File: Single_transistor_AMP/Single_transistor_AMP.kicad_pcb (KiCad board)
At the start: 2 copper layers, 0 parts

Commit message: Majasdarbs peec 8. lekcijas, kur jauzzimee plate
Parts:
- added C1: 1 uF, Capacitors_THT:CP_Axial_L10.0mm_D4.5mm_P15.00mm_Horizontal, F.Cu at (98.2, 145.4)
- added C2: 20 uF, Capacitors_THT:CP_Radial_D10.0mm_P2.50mm, F.Cu at (112.3, 127.6)
- added J1: Barosana un ieeja, Connectors:AK300-4, F.Cu at (113.7, 154.8)
- added J2: Izeja, Connectors:AK300-2, F.Cu at (95.5, 126.7)
- added J3: Stiprinajums1, Mounting_Holes:MountingHole_2.2mm_M2_Pad, F.Cu at (121.7, 146.1)
- added J4: Stiprinajums2, Mounting_Holes:MountingHole_2.2mm_M2_Pad, F.Cu at (93.5, 145.4)
- added J5: Stiprinajums3, Mounting_Holes:MountingHole_2.2mm_M2_Pad, F.Cu at (106.8, 122.8)
- added Q1: BC547, TO_SOT_Packages_THT:TO-92_Molded_Narrow, F.Cu at (106.3, 138.2)
- added R1: 4.7 k, Resistors_THT:R_Axial_DIN0204_L3.6mm_D1.6mm_P7.62mm_Horizontal, F.Cu at (86.4, 141.2)
- added R2: 1k, Resistors_THT:R_Axial_DIN0207_L6.3mm_D2.5mm_P10.16mm_Horizontal, F.Cu at (124.5, 141.6)
- added R3: 4.7 k, Resistors_THT:R_Axial_DIN0204_L3.6mm_D1.6mm_P7.62mm_Horizontal, F.Cu at (86.4, 135.9)
- added R4: 1 k, Resistors_THT:R_Axial_DIN0207_L6.3mm_D2.5mm_P10.16mm_Horizontal, F.Cu at (124.5, 136.7)
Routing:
- net Net-(C1-Pad1): track 0.00 -> 43.6 mm
- net Net-(C2-Pad2): track 0.00 -> 28.4 mm
- net +9V: track 0.00 -> 25.9 mm
- net Net-(J2-Pad1): track 0.00 -> 25.3 mm
- net Net-(C1-Pad2): track 0.00 -> 9.61 mm
- added copper zone on B.Cu, net GND
- added copper zone on F.Cu, net GND
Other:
- board outline added: 50 x 43.3 mm

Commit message: Single_transistor_AMP 2. iteraacija
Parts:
- C1: footprint Capacitors_THT:CP_Axial_L10.0mm_D4.5mm_P15.00mm_Horizontal -> Capacitors_THT:C_Rect_L10.0mm_W2.5mm_P7.50mm_MKS4
- C2: footprint Capacitors_THT:CP_Radial_D10.0mm_P2.50mm -> Capacitors_THT:C_Rect_L10.0mm_W2.5mm_P7.50mm_MKS4
- moved R4 10.5 mm to (113.9, 136.9), turned to 0 degrees
- moved R2 10.4 mm to (114.0, 141.5), turned to 0 degrees
- moved C2 10.3 mm to (122.2, 130.3), turned to 180 degrees
- moved C1 5.58 mm to (103.2, 143.1)
- moved J4 4.05 mm to (90.8, 148.5), turned to 0 degrees
- moved J3 2.50 mm to (121.0, 148.5), turned to 0 degrees
- moved J5 1.45 mm to (108.2, 122.4)
- moved Q1 0.80 mm to (106.6, 137.4)
- moved J1 0.51 mm to (113.7, 154.3)
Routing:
- net Net-(C2-Pad2): track 28.4 -> 12.0 mm
- net Net-(C1-Pad1): track 43.6 -> 27.2 mm
- net Net-(J2-Pad1): track 25.3 -> 23.0 mm
- net Net-(C1-Pad2): track 9.61 -> 11.4 mm
- net +9V: track 25.9 -> 24.4 mm

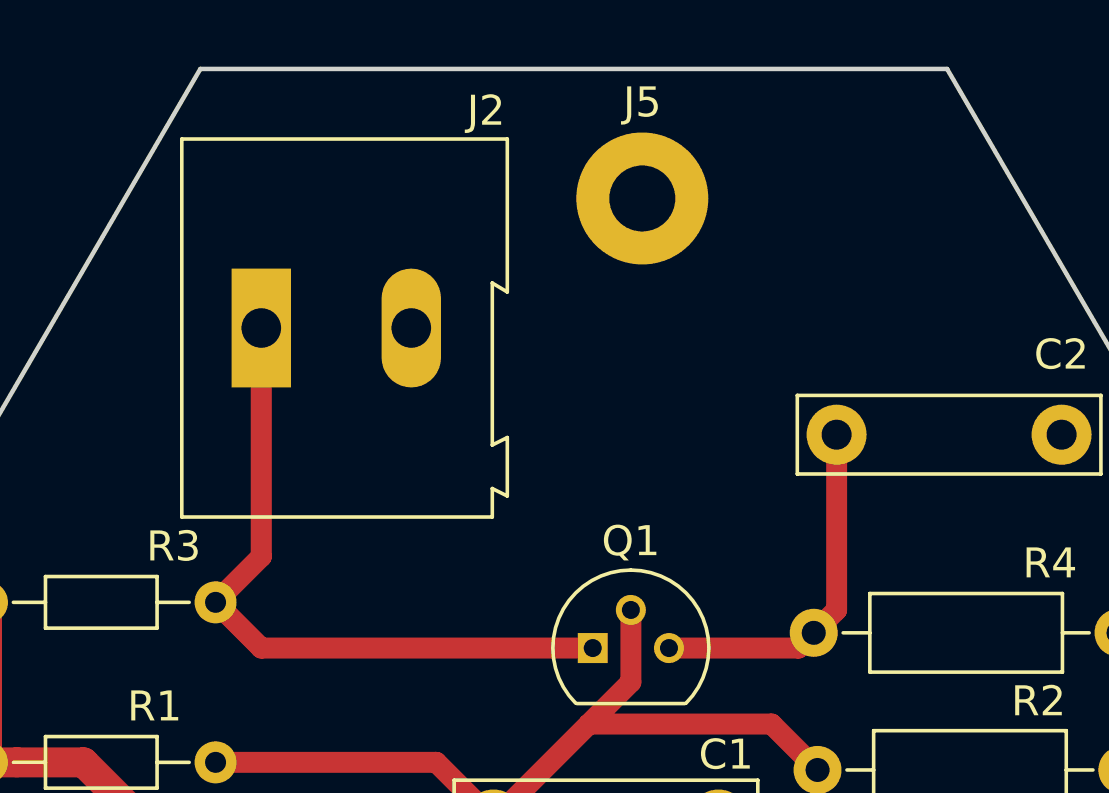
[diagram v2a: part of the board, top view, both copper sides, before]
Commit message: Single transistor AMP 2. iteraacija
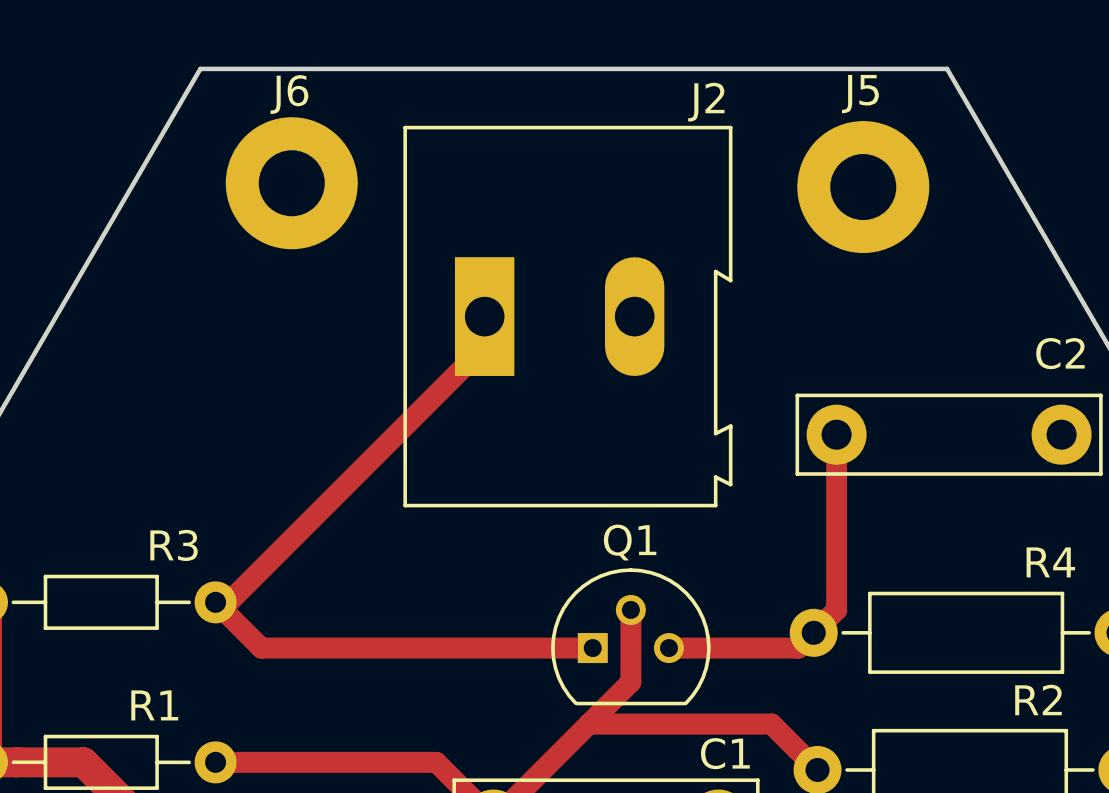
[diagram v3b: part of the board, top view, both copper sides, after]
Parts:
- added J6: Stiprinajums4, Mounting_Holes:MountingHole_2.2mm_M2_Pad, F.Cu at (96.5, 121.9)
- moved J2 7.46 mm to (103.0, 126.4)
- moved J5 7.38 mm to (115.6, 122.0)
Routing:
- net Net-(J2-Pad1): track 23.0 -> 26.7 mm
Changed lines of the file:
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@@
 (kicad_pcb (version 4) (host pcbnew 4.0.7)
   (general
-    (links 18)
+    (links 19)
     (no_connects 0)
     (area 80.823999 118.034999 131.012001 161.492001)
     (thickness 1.6)
     (drawings 6)
-    (tracks 22)
+    (tracks 23)
     (zones 0)
-    (modules 12)
+    (modules 13)
     (nets 7)
   )
@@
   )
   (module Connectors:AK300-2 (layer F.Cu)
-    (at 95.504 126.746)
+    (at 102.95 126.365)
     (descr CONNECTOR)
     (tags CONNECTOR)
@@
   )
   (module Mounting_Holes:MountingHole_2.2mm_M2_Pad (layer F.Cu)
-    (at 108.204 122.428)
+    (at 115.57 122.047)
     (descr "Mounting Hole 2.2mm, M2")
     (tags "mounting hole 2.2mm m2")
@@
       (rotate (xyz 0 0 0))
     )
+  )
+  (module Mounting_Holes:MountingHole_2.2mm_M2_Pad (layer F.Cu)
+    (at 96.52 121.92)
+    (descr "Mounting Hole 2.2mm, M2")
+    (tags "mounting hole 2.2mm m2")
+    (fp_text reference J6 (at 0 -3.048) (layer F.SilkS)
+      (effects (font (size 1 1) (thickness 0.15)))
+    )
+    (fp_text value Stiprinajums4 (at 0 3.2) (layer F.Fab)
+      (effects (font (size 1 1) (thickness 0.15)))
+    )
+    (fp_circle (center 0 0) (end 2.2 0) (layer Cmts.User) (width 0.15))
+    (fp_circle (center 0 0) (end 2.45 0) (layer F.CrtYd) (width 0.05))
+    (pad 1 thru_hole circle (at 0 0) (size 4.4 4.4) (drill 2.2) (layers *.Cu *.Mask)
+      (net 3 GND))
   )
   (gr_line (start 80.899 139.7) (end 93.472 118.11) (layer Edge.Cuts) (width 0.15))
@@
   (segment (start 87.349949 141.224) (end 86.36 141.224) (width 1) (layer F.Cu) (net 5))
   (segment (start 86.36 135.89) (end 86.36 141.224) (width 1) (layer F.Cu) (net 5))
+  (segment (start 102.95 126.365) (end 102.95 127.355) (width 0.7) (layer F.Cu) (net 6))
+  (segment (start 102.95 127.355) (end 94.415 135.89) (width 0.7) (layer F.Cu) (net 6))
+  (segment (start 94.415 135.89) (end 93.98 135.89) (width 0.7) (layer F.Cu) (net 6))
   (segment (start 93.98 135.89) (end 95.504 137.414) (width 0.7) (layer F.Cu) (net 6))
   (segment (start 95.504 137.414) (end 106.553 137.414) (width 0.7) (layer F.Cu) (net 6))
-  (segment (start 95.504 126.746) (end 95.504 134.366) (width 0.7) (layer F.Cu) (net 6))
-  (segment (start 95.504 134.366) (end 93.98 135.89) (width 0.7) (layer F.Cu) (net 6))
   (zone (net 3) (net_name GND) (layer F.Cu) (hatch edge 0.508)
     (connect_pads (clearance 0.2))
     (min_thickness 0.254)
-    (fill yes (arc_segments 16) (thermal_gap 0.2) (thermal_bridge_width 0.508))
+    (fill (arc_segments 16) (thermal_gap 0.2) (thermal_bridge_width 0.508))
     (polygon
       (pts
@@
     (connect_pads (clearance 0.3))
     (min_thickness 0.254)
-    (fill yes (arc_segments 16) (thermal_gap 0.3) (thermal_bridge_width 0.508))
+    (fill (arc_segments 16) (thermal_gap 0.3) (thermal_bridge_width 0.508))
     (polygon
       (pts
